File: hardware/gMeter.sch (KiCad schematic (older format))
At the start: 45 parts, among them IC1 ATMEGA88P, K1 CONN_3, P4 USB, P5 ISP, Q1 BC548, U1 LN-6206-30, X1 12MHz

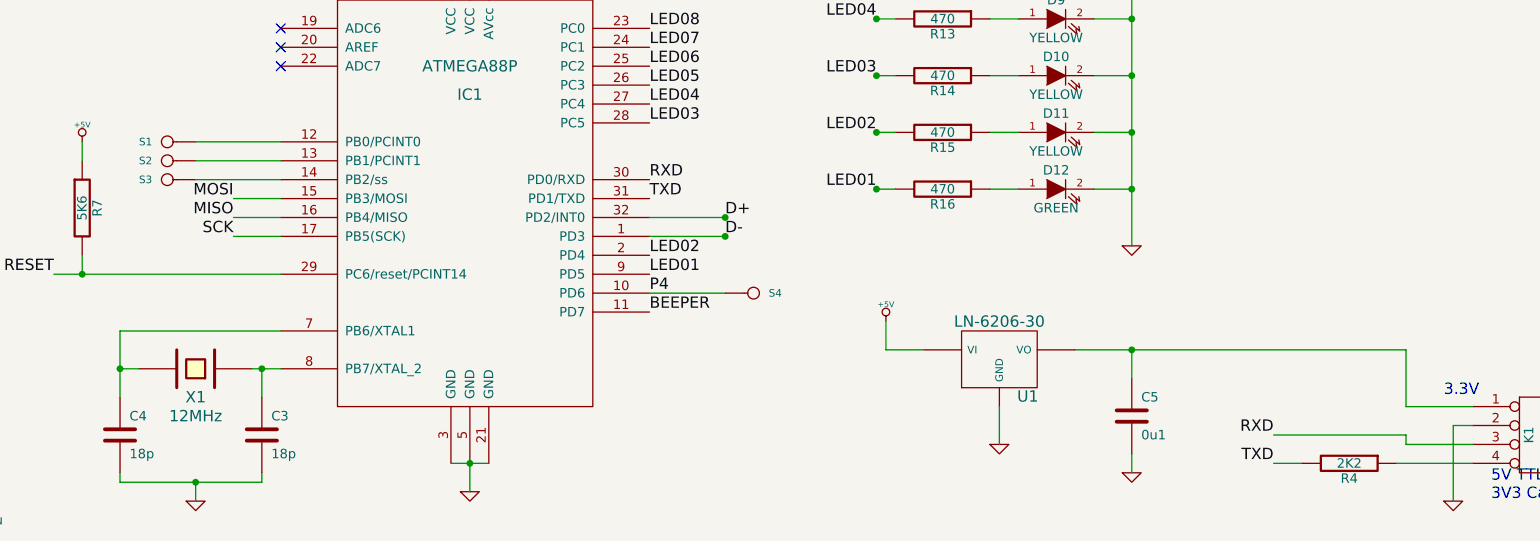
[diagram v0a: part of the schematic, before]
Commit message: + A bunch of module and 3d package tidying and corrections work. + Consolidated all parts modules int gruvin.mod/mdc. Deleted others. + Subsequent changes and corrections to module names on the two PCBs. + Tidied up silk layers on boath boads.
NOTE: Left version at v1.0. (Previous production version should have been 0.2 *shrug*)

NOTE: This gruvin.mod/mdc module library is the latest and most "correct" version for all my projects. I will eventually place a copy somewhere as a master, for future projects.
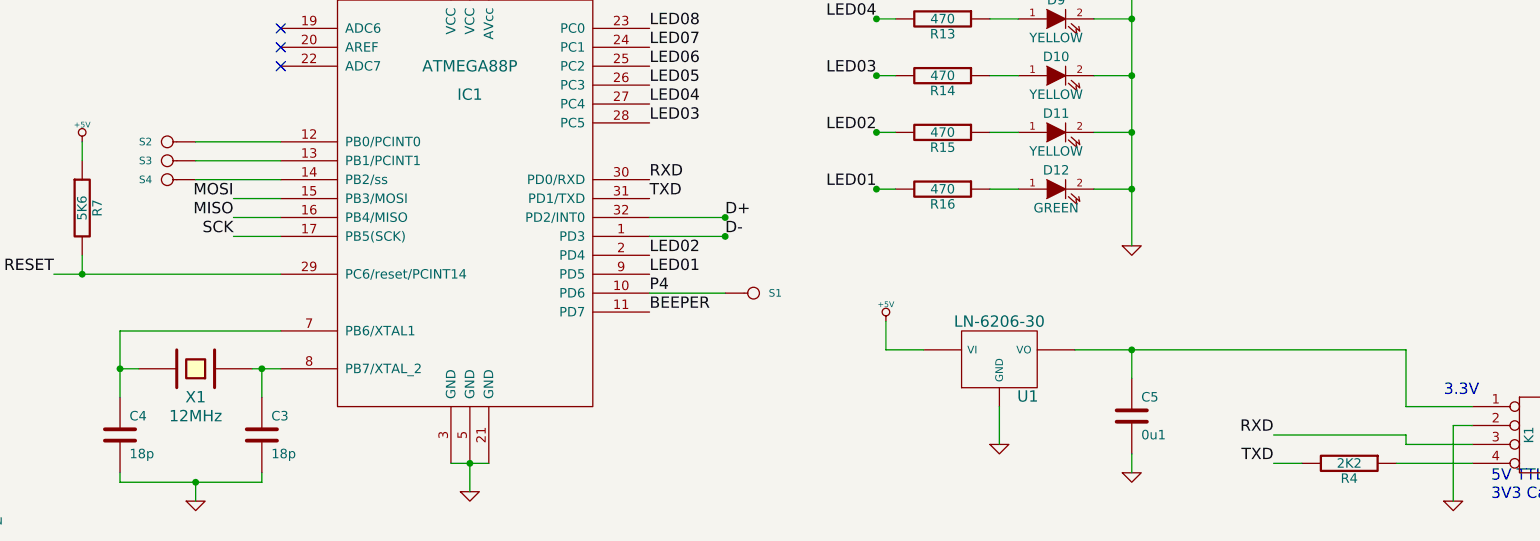
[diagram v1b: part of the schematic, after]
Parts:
- renumbered S4 to S1, S1 to S2, S2 to S3, S3 to S4
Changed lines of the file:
@@
 LIBS:atmega48p
 LIBS:beeper
-LIBS:tMeter-cache
+LIBS:gMeter-cache
 EELAYER 24 0
 EELAYER END
@@
 	9350 6300 9000 6300
 Wire Wire Line
-	9000 6000 9000 6300
-Wire Wire Line
-	7250 6000 9000 6000
+	9000 6300 9000 6000
+Wire Wire Line
+	9000 6000 7250 6000
 Wire Wire Line
 	8300 6450 9000 6450
@@
 $EndComp
 $Comp
-L CONN_1 S4
+L CONN_1 S1
 U 1 1 51A9A872
 P 5550 5700
-F 0 "S4" H 5630 5700 40  0000 L CNN
+F 0 "S1" H 5630 5700 40  0000 L CNN
 F 1 "CONN_1" H 5550 5755 30  0001 C CNN
 F 2 "" H 5550 5700 60  0001 C CNN
@@
 3x2 pogo\npin pads
 $Comp
-L CONN_1 S3
+L CONN_1 S4
 U 1 1 51A74C00
 P 2450 5100
-F 0 "S3" H 2530 5100 40  0000 L CNN
+F 0 "S4" H 2530 5100 40  0000 L CNN
 F 1 "CONN_1" H 2450 5155 30  0001 C CNN
 F 2 "" H 2450 5100 60  0001 C CNN
@@
 $EndComp
 $Comp
-L CONN_1 S2
+L CONN_1 S3
 U 1 1 51A74BFE
 P 2450 5000
-F 0 "S2" H 2530 5000 40  0000 L CNN
+F 0 "S3" H 2530 5000 40  0000 L CNN
 F 1 "CONN_1" H 2450 5055 30  0001 C CNN
 F 2 "" H 2450 5000 60  0001 C CNN
@@
 $EndComp
 $Comp
-L CONN_1 S1
+L CONN_1 S2
 U 1 1 51A74BE2
 P 2450 4900
-F 0 "S1" H 2530 4900 40  0000 L CNN
+F 0 "S2" H 2530 4900 40  0000 L CNN
 F 1 "CONN_1" H 2450 4955 30  0001 C CNN
 F 2 "" H 2450 4900 60  0001 C CNN

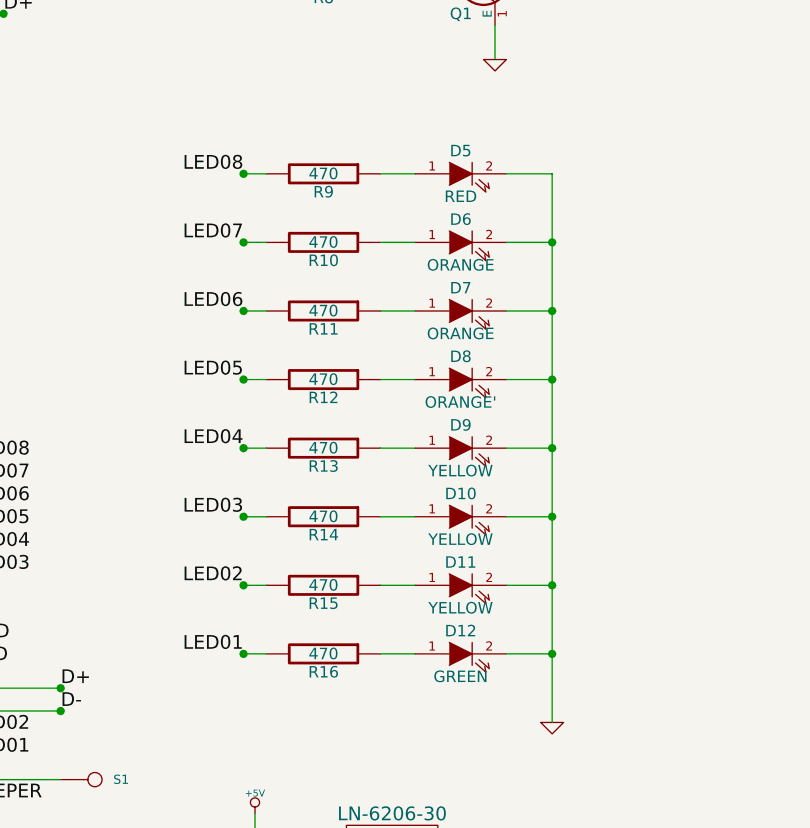
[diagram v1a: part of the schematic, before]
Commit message: Changed the schematic and PCB to match the final LED selection ...
Green, Green, Yellow, Yellow, Yellow, Orange, Orange, Red

Changed resistors for green and red LED's, because they were too bright 
-- especially the green ones.
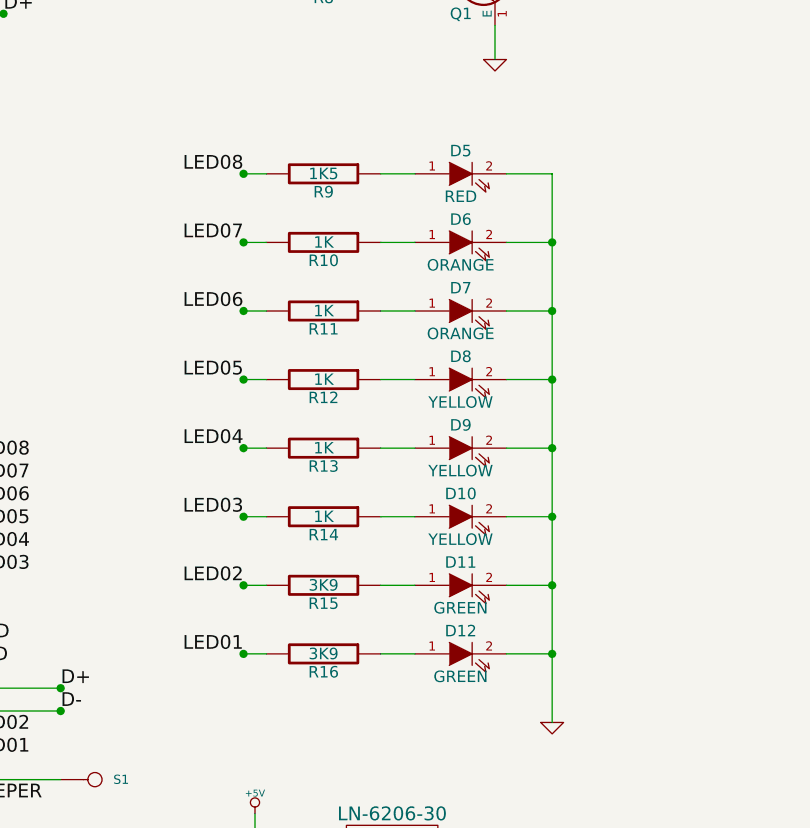
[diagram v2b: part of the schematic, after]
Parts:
- D11: value YELLOW -> GREEN
- D8: value ORANGE' -> YELLOW
- R10, R11, R12, R13, R14: value 470 -> 1K
- R15, R16: value 470 -> 3K9
- R9: value 470 -> 1K5
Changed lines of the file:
@@
 P 6550 5150
 F 0 "R16" V 6630 5150 50  0000 C CNN
-F 1 "470" V 6550 5150 50  0000 C CNN
+F 1 "3K9" V 6550 5150 50  0000 C CNN
 F 2 "" H 6550 5150 60  0001 C CNN
 F 3 "" H 6550 5150 60  0001 C CNN
@@
 P 6550 4850
 F 0 "R15" V 6630 4850 50  0000 C CNN
-F 1 "470" V 6550 4850 50  0000 C CNN
+F 1 "3K9" V 6550 4850 50  0000 C CNN
 F 2 "" H 6550 4850 60  0001 C CNN
 F 3 "" H 6550 4850 60  0001 C CNN
@@
 P 6550 4550
 F 0 "R14" V 6630 4550 50  0000 C CNN
-F 1 "470" V 6550 4550 50  0000 C CNN
+F 1 "1K" V 6550 4550 50  0000 C CNN
 F 2 "" H 6550 4550 60  0001 C CNN
 F 3 "" H 6550 4550 60  0001 C CNN
@@
 P 6550 4250
 F 0 "R13" V 6630 4250 50  0000 C CNN
-F 1 "470" V 6550 4250 50  0000 C CNN
+F 1 "1K" V 6550 4250 50  0000 C CNN
 F 2 "" H 6550 4250 60  0001 C CNN
 F 3 "" H 6550 4250 60  0001 C CNN
@@
 P 6550 3950
 F 0 "R12" V 6630 3950 50  0000 C CNN
-F 1 "470" V 6550 3950 50  0000 C CNN
+F 1 "1K" V 6550 3950 50  0000 C CNN
 F 2 "" H 6550 3950 60  0001 C CNN
 F 3 "" H 6550 3950 60  0001 C CNN
@@
 P 6550 3650
 F 0 "R11" V 6630 3650 50  0000 C CNN
-F 1 "470" V 6550 3650 50  0000 C CNN
+F 1 "1K" V 6550 3650 50  0000 C CNN
 F 2 "" H 6550 3650 60  0001 C CNN
 F 3 "" H 6550 3650 60  0001 C CNN
@@
 P 6550 3350
 F 0 "R10" V 6630 3350 50  0000 C CNN
-F 1 "470" V 6550 3350 50  0000 C CNN
+F 1 "1K" V 6550 3350 50  0000 C CNN
 F 2 "" H 6550 3350 60  0001 C CNN
 F 3 "" H 6550 3350 60  0001 C CNN
@@
 P 6550 3050
 F 0 "R9" V 6630 3050 50  0000 C CNN
-F 1 "470" V 6550 3050 50  0000 C CNN
+F 1 "1K5" V 6550 3050 50  0000 C CNN
 F 2 "" H 6550 3050 60  0001 C CNN
 F 3 "" H 6550 3050 60  0001 C CNN
@@
 P 7150 4850
 F 0 "D11" H 7150 4950 50  0000 C CNN
-F 1 "YELLOW" H 7150 4750 50  0000 C CNN
+F 1 "GREEN" H 7150 4750 50  0000 C CNN
 F 2 "" H 7150 4850 60  0001 C CNN
 F 3 "" H 7150 4850 60  0001 C CNN
@@
 P 7150 3950
 F 0 "D8" H 7150 4050 50  0000 C CNN
-F 1 "ORANGE'" H 7150 3850 50  0000 C CNN
+F 1 "YELLOW" H 7150 3850 50  0000 C CNN
 F 2 "" H 7150 3950 60  0001 C CNN
 F 3 "" H 7150 3950 60  0001 C CNN
